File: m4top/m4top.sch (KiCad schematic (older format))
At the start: 7 parts, among them J1 WEST TOP, J2 EAST TOP

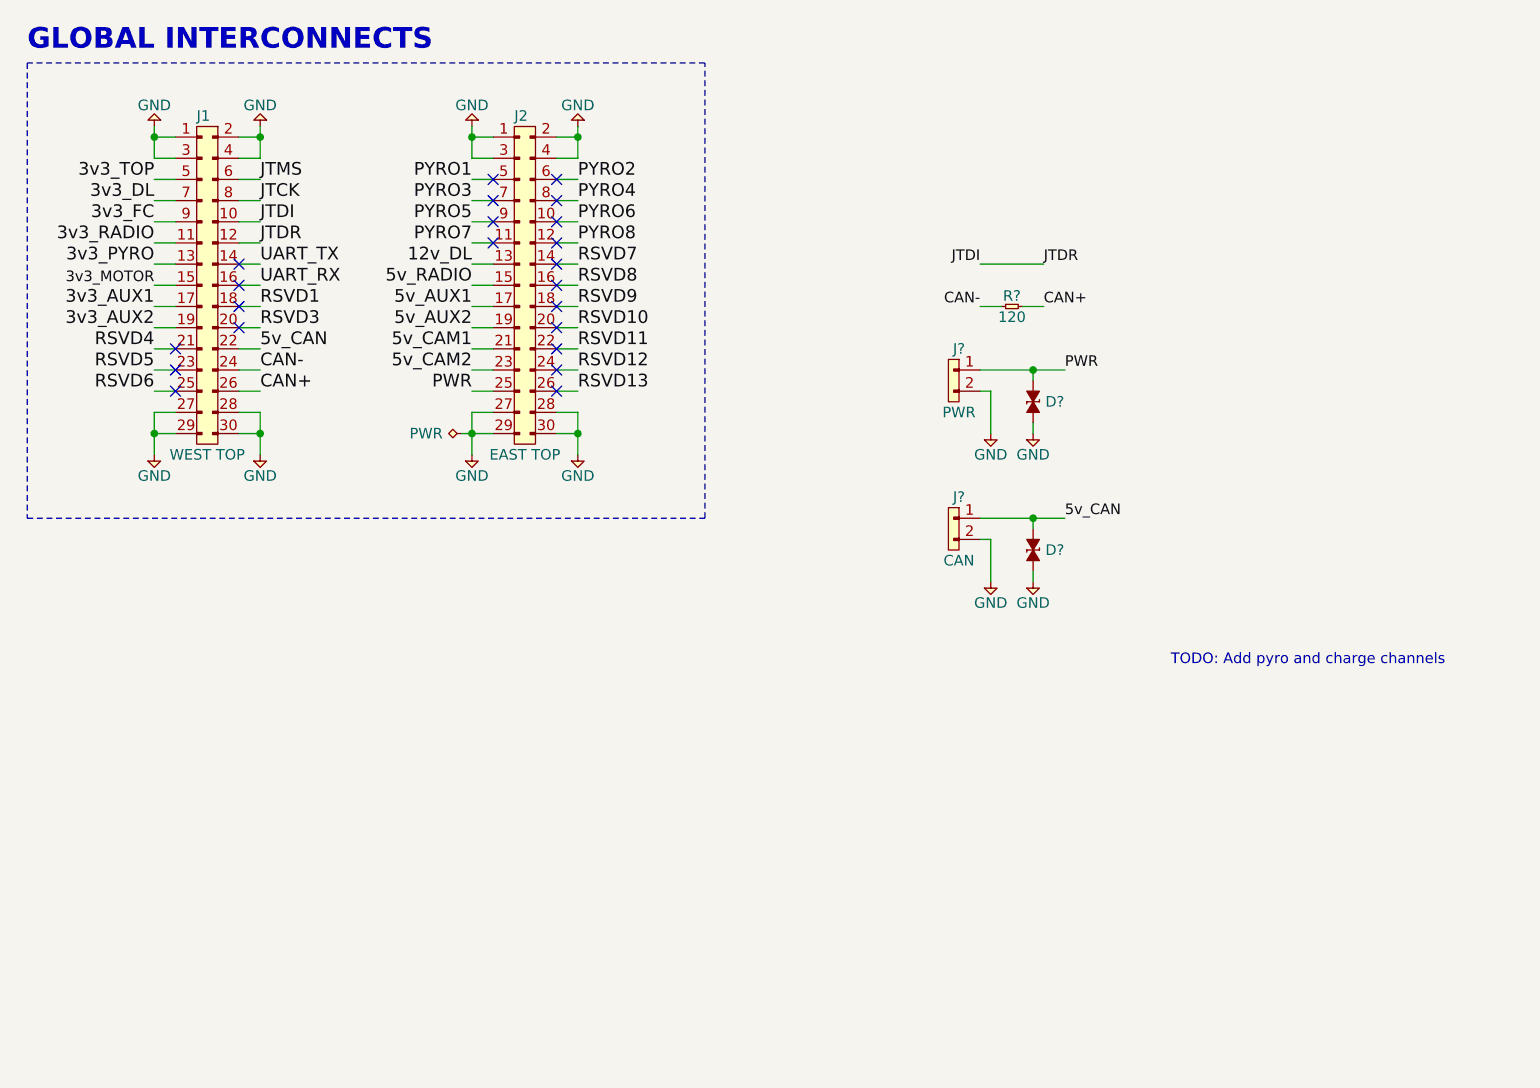
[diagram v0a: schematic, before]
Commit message: Revise global interconnects
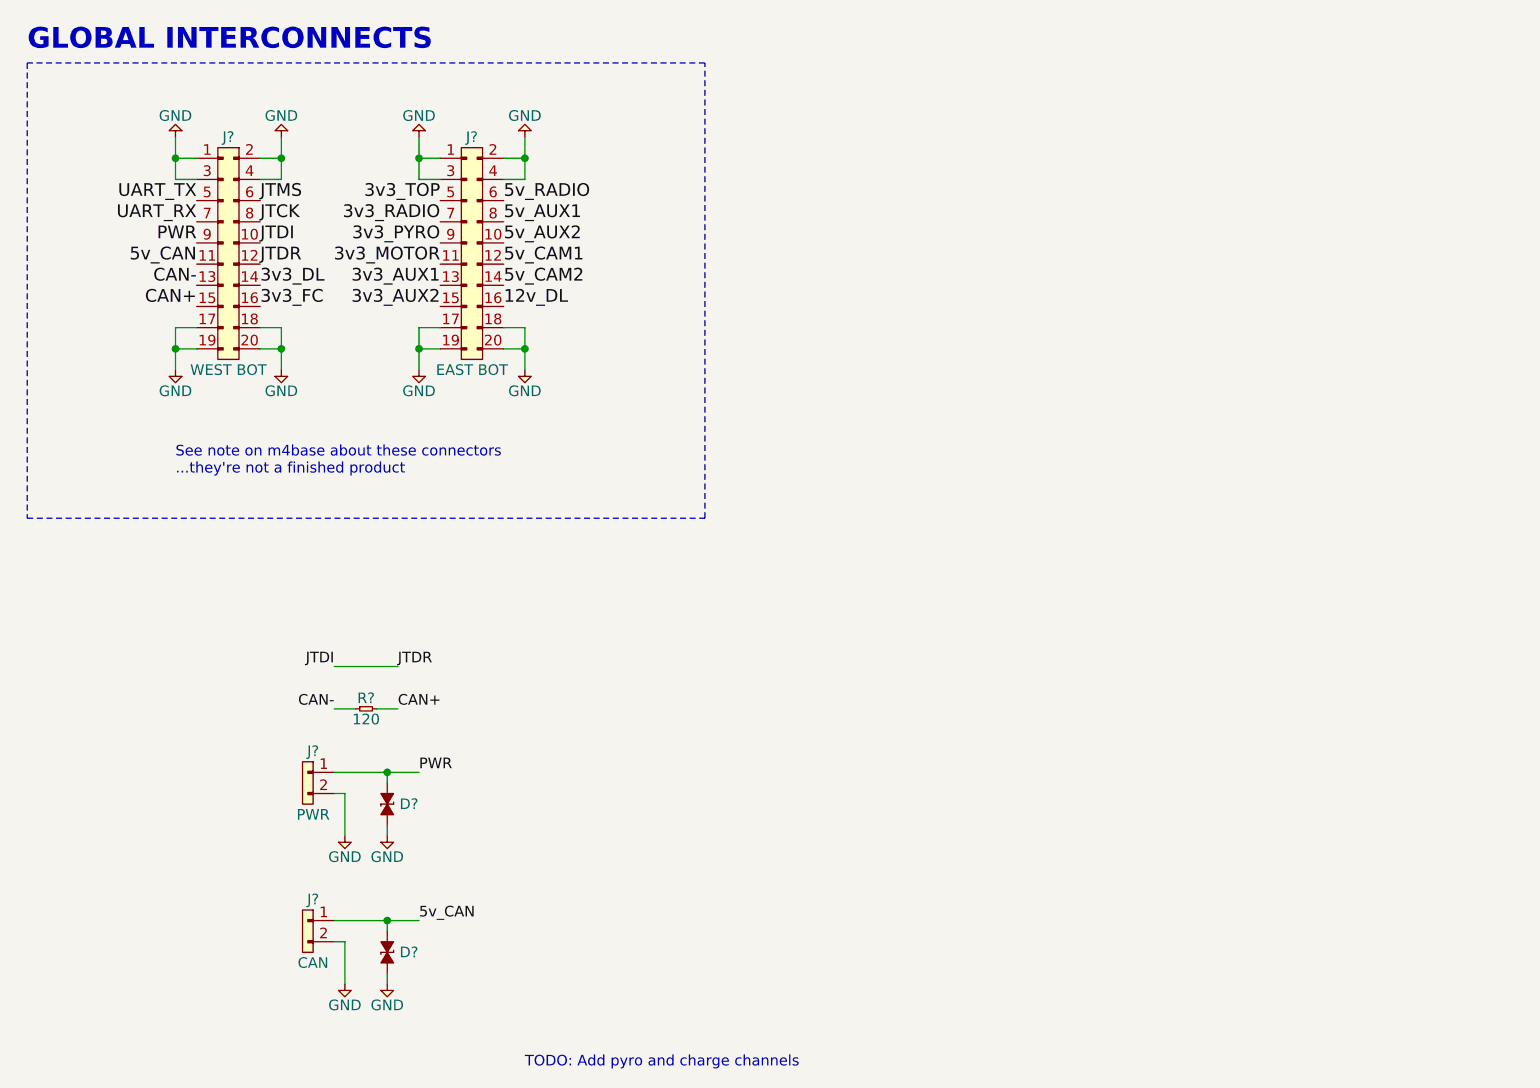
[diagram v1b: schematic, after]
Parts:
- removed J1: WEST TOP, agg:TFML-115-02-L-D-LC, symbol cusf-kicad:CONN_02x15
- removed J2: EAST TOP, agg:TFML-115-02-L-D-LC, symbol cusf-kicad:CONN_02x15
- added J?: WEST BOT, symbol cusf-kicad:CONN_02x10
- added J?: EAST BOT, symbol cusf-kicad:CONN_02x10
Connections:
- net 12v_DL: now also J?.16
- net 3v3_AUX1: now also J?.13
- net 3v3_AUX2: now also J?.15
- net 3v3_DL: now also J?.14
- net 3v3_FC: now also J?.16
- net 3v3_MOTOR: now also J?.11
- net 3v3_PYRO: now also J?.9
- net 3v3_RADIO: now also J?.7
- net 3v3_TOP: now also J?.5
- net 5v_AUX1: now also J?.8
- net 5v_AUX2: now also J?.10
- net 5v_CAM1: now also J?.12
- net 5v_CAM2: now also J?.14
- net 5v_CAN: now also J?.11
- net 5v_RADIO: now also J?.6
- net CAN+: now also J?.15
- net CAN-: now also J?.13
- net GND: now also J?.1, J?.1, J?.17, J?.17, J?.18, J?.18, J?.19, J?.19, J?.2, J?.2, J?.20, J?.20, J?.3, J?.3, J?.4, J?.4
- net JTCK: now also J?.8
- net JTDI: now also J?.10, J?.12
- net JTMS: now also J?.6
- net PWR: now also J?.9
- net UART_RX: now also J?.7
- net UART_TX: now also J?.5
- no-connect marks 22 -> 0
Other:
- note added: "See note on m4base about these connectors\n...they're not a finished product"
- moved on the sheet: D?, J?, R?

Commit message: Cleanup
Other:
- note added: "CAN Link"
- note added: "External Interconnects"
- note added: "JTAG Link"
- note removed: "TODO: Add pyro and charge channels"
- moved on the sheet: D?, J?, R?
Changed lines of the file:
@@
 JTDR
 Wire Notes Line
-	650  2950 3850 2950
+	600  2950 3800 2950
 Wire Notes Line
 	3850 2950 3850 800
@@
 Text Label 2600 1750 2    60   ~ 0
 3v3_MOTOR
-Text Label 2100 3650 2    50   ~ 0
+Text Label 1000 3250 2    50   ~ 0
 JTDI
-Text Label 2400 3650 0    50   ~ 0
+Text Label 1300 3250 0    50   ~ 0
 JTDR
 Wire Wire Line
-	2400 3650 2100 3650
-Text Label 2100 3850 2    50   ~ 0
+	1300 3250 1000 3250
+Text Label 1000 3800 2    50   ~ 0
 CAN-
-Text Label 2400 3850 0    50   ~ 0
+Text Label 1300 3800 0    50   ~ 0
 CAN+
 Wire Wire Line
-	2400 3850 2300 3850
-Wire Wire Line
-	2200 3850 2100 3850
+	1300 3800 1200 3800
+Wire Wire Line
+	1100 3800 1000 3800
 $Comp
 L cusf-kicad:R R?
 U 1 1 5EE1EB7B
-P 2200 3850
-F 0 "R?" H 2250 3900 50  0000 C CNN
-F 1 "120" H 2250 3800 50  0000 C CNN
-F 2 "" H 2200 3850 50  0001 C CNN
-F 3 "" H 2200 3850 50  0001 C CNN
-	1    2200 3850
-	1    0    0    -1
-$EndComp
-Text Notes 3000 5550 0    50   ~ 0
-TODO: Add pyro and charge channels
+P 1100 3800
+F 0 "R?" H 1150 3850 50  0000 C CNN
+F 1 "120" H 1150 3750 50  0000 C CNN
+F 2 "" H 1100 3800 50  0001 C CNN
+F 3 "" H 1100 3800 50  0001 C CNN
+	1    1100 3800
+	1    0    0    -1
+$EndComp
 $Comp
 L cusf-kicad:CONN_01x02 J?
 U 1 1 5EE256C6
-P 2000 4150
-F 0 "J?" H 2000 4250 50  0000 C CNN
-F 1 "PWR" H 2000 3950 50  0000 C CNN
-F 2 "" H 2000 4150 50  0001 C CNN
-F 3 "" H 2000 4150 50  0001 C CNN
-	1    2000 4150
+P 2000 3350
+F 0 "J?" H 2000 3450 50  0000 C CNN
+F 1 "PWR" H 2000 3150 50  0000 C CNN
+F 2 "" H 2000 3350 50  0001 C CNN
+F 3 "" H 2000 3350 50  0001 C CNN
+	1    2000 3350
 	1    0    0    -1
 $EndComp
@@
 L cusf-kicad:CONN_01x02 J?
 U 1 1 5EE258D0
-P 2000 4850
-F 0 "J?" H 2000 4950 50  0000 C CNN
-F 1 "CAN" H 2000 4650 50  0000 C CNN
-F 2 "" H 2000 4850 50  0001 C CNN
-F 3 "" H 2000 4850 50  0001 C CNN
-	1    2000 4850
-	1    0    0    -1
-$EndComp
-Wire Wire Line
-	2150 5150 2150 4950
-Wire Wire Line
-	2150 4950 2100 4950
-Wire Wire Line
-	2350 5150 2350 5100
-Wire Wire Line
-	2350 4900 2350 4850
-Wire Wire Line
-	2350 4850 2100 4850
-Wire Wire Line
-	2350 4850 2500 4850
-Connection ~ 2350 4850
-Text Label 2500 4850 0    50   ~ 0
+P 2900 3350
+F 0 "J?" H 2900 3450 50  0000 C CNN
+F 1 "CAN" H 2900 3150 50  0000 C CNN
+F 2 "" H 2900 3350 50  0001 C CNN
+F 3 "" H 2900 3350 50  0001 C CNN
+	1    2900 3350
+	1    0    0    -1
+$EndComp
+Wire Wire Line
+	3050 3650 3050 3450
+Wire Wire Line
+	3050 3450 3000 3450
+Wire Wire Line
+	3250 3650 3250 3600
+Wire Wire Line
+	3250 3400 3250 3350
+Wire Wire Line
+	3250 3350 3000 3350
+Wire Wire Line
+	3250 3350 3400 3350
+Connection ~ 3250 3350
+Text Label 3400 3350 0    50   ~ 0
 5v_CAN
 $Comp
 L cusf-kicad:ESD_DIODE D?
 U 1 1 5EE2FB70
-P 2350 5000
-F 0 "D?" V 2350 5058 50  0000 L CNN
-F 1 "ESD_DIODE" H 2300 4900 50  0001 L CNN
-F 2 "agg:0402" H 2300 4800 50  0001 L CNN
-F 3 "" H 2250 5000 50  0001 C CNN
-F 4 "2368169" H 2300 4700 50  0001 L CNN "Farnell"
-	1    2350 5000
+P 3250 3500
+F 0 "D?" V 3250 3558 50  0000 L CNN
+F 1 "ESD_DIODE" H 3200 3400 50  0001 L CNN
+F 2 "agg:0402" H 3200 3300 50  0001 L CNN
+F 3 "" H 3150 3500 50  0001 C CNN
+F 4 "2368169" H 3200 3200 50  0001 L CNN "Farnell"
+	1    3250 3500
 	0    1    1    0
 $EndComp
@@
 L cusf-kicad:GND #PWR?
 U 1 1 5EE2FF8C
-P 2350 5150
-F 0 "#PWR?" H 2220 5190 50  0001 L CNN
-F 1 "GND" H 2350 5050 50  0000 C CNN
-F 2 "" H 2350 5150 50  0001 C CNN
-F 3 "" H 2350 5150 50  0001 C CNN
-	1    2350 5150
+P 3250 3650
+F 0 "#PWR?" H 3120 3690 50  0001 L CNN
+F 1 "GND" H 3250 3550 50  0000 C CNN
+F 2 "" H 3250 3650 50  0001 C CNN
+F 3 "" H 3250 3650 50  0001 C CNN
+	1    3250 3650
 	1    0    0    -1
 $EndComp
@@
 L cusf-kicad:GND #PWR?
 U 1 1 5EE30203
-P 2150 5150
-F 0 "#PWR?" H 2020 5190 50  0001 L CNN
-F 1 "GND" H 2150 5050 50  0000 C CNN
-F 2 "" H 2150 5150 50  0001 C CNN
-F 3 "" H 2150 5150 50  0001 C CNN
-	1    2150 5150
-	1    0    0    -1
-$EndComp
-Wire Wire Line
-	2150 4450 2150 4250
-Wire Wire Line
-	2150 4250 2100 4250
-Wire Wire Line
-	2350 4450 2350 4400
-Wire Wire Line
-	2350 4200 2350 4150
-Wire Wire Line
-	2350 4150 2100 4150
-Wire Wire Line
-	2350 4150 2500 4150
-Connection ~ 2350 4150
+P 3050 3650
+F 0 "#PWR?" H 2920 3690 50  0001 L CNN
+F 1 "GND" H 3050 3550 50  0000 C CNN
+F 2 "" H 3050 3650 50  0001 C CNN
+F 3 "" H 3050 3650 50  0001 C CNN
+	1    3050 3650
+	1    0    0    -1
+$EndComp
+Wire Wire Line
+	2150 3650 2150 3450
+Wire Wire Line
+	2150 3450 2100 3450
+Wire Wire Line
+	2350 3650 2350 3600
+Wire Wire Line
+	2350 3400 2350 3350
+Wire Wire Line
+	2350 3350 2100 3350
+Wire Wire Line
+	2350 3350 2500 3350
+Connection ~ 2350 3350
 $Comp
 L cusf-kicad:ESD_DIODE D?
 U 1 1 5EE33074
-P 2350 4300
-F 0 "D?" V 2350 4358 50  0000 L CNN
-F 1 "ESD_DIODE" H 2300 4200 50  0001 L CNN
-F 2 "agg:0402" H 2300 4100 50  0001 L CNN
-F 3 "" H 2250 4300 50  0001 C CNN
-F 4 "2368169" H 2300 4000 50  0001 L CNN "Farnell"
-	1    2350 4300
+P 2350 3500
+F 0 "D?" V 2350 3558 50  0000 L CNN
+F 1 "ESD_DIODE" H 2300 3400 50  0001 L CNN
+F 2 "agg:0402" H 2300 3300 50  0001 L CNN
+F 3 "" H 2250 3500 50  0001 C CNN
+F 4 "2368169" H 2300 3200 50  0001 L CNN "Farnell"
+	1    2350 3500
 	0    1    1    0
 $EndComp
@@
 L cusf-kicad:GND #PWR?
 U 1 1 5EE3307A
-P 2350 4450
-F 0 "#PWR?" H 2220 4490 50  0001 L CNN
-F 1 "GND" H 2350 4350 50  0000 C CNN
-F 2 "" H 2350 4450 50  0001 C CNN
-F 3 "" H 2350 4450 50  0001 C CNN
-	1    2350 4450
+P 2350 3650
+F 0 "#PWR?" H 2220 3690 50  0001 L CNN
+F 1 "GND" H 2350 3550 50  0000 C CNN
+F 2 "" H 2350 3650 50  0001 C CNN
+F 3 "" H 2350 3650 50  0001 C CNN
+	1    2350 3650
 	1    0    0    -1
 $EndComp
@@
 L cusf-kicad:GND #PWR?
 U 1 1 5EE33080
-P 2150 4450
-F 0 "#PWR?" H 2020 4490 50  0001 L CNN
-F 1 "GND" H 2150 4350 50  0000 C CNN
-F 2 "" H 2150 4450 50  0001 C CNN
-F 3 "" H 2150 4450 50  0001 C CNN
-	1    2150 4450
-	1    0    0    -1
-$EndComp
-Text Label 2500 4150 0    50   ~ 0
+P 2150 3650
+F 0 "#PWR?" H 2020 3690 50  0001 L CNN
+F 1 "GND" H 2150 3550 50  0000 C CNN
+F 2 "" H 2150 3650 50  0001 C CNN
+F 3 "" H 2150 3650 50  0001 C CNN
+	1    2150 3650
+	1    0    0    -1
+$EndComp
+Text Label 2500 3350 0    50   ~ 0
 PWR
 $Comp
@@
 Text Notes 1350 2750 0    50   ~ 0
 See note on m4base about these connectors\n...they're not a finished product
+Wire Notes Line
+	650  3100 1650 3100
+Wire Notes Line
+	1650 3550 650  3550
+Text Notes 700  3500 0    60   ~ 0
+JTAG Link
+Wire Notes Line
+	1650 3100 1650 3550
+Wire Notes Line
+	650  3100 650  3550
+Wire Notes Line
+	650  3650 650  4100
+Wire Notes Line
+	650  4100 1650 4100
+Wire Notes Line
+	1650 4100 1650 3650
+Wire Notes Line
+	1650 3650 650  3650
+Text Notes 700  4050 0    60   ~ 0
+CAN Link
+Wire Notes Line
+	1750 3100 3850 3100
+Wire Notes Line
+	3850 3100 3850 4100
+Wire Notes Line
+	3850 4100 1750 4100
+Wire Notes Line
+	1750 3100 1750 4100
+Text Notes 1800 4050 0    60   ~ 0
+External Interconnects
 $EndSCHEMATC
